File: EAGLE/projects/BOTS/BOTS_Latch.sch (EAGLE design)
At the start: 5 parts, among them J1 T821108A1S100CEU, K1 RT444012

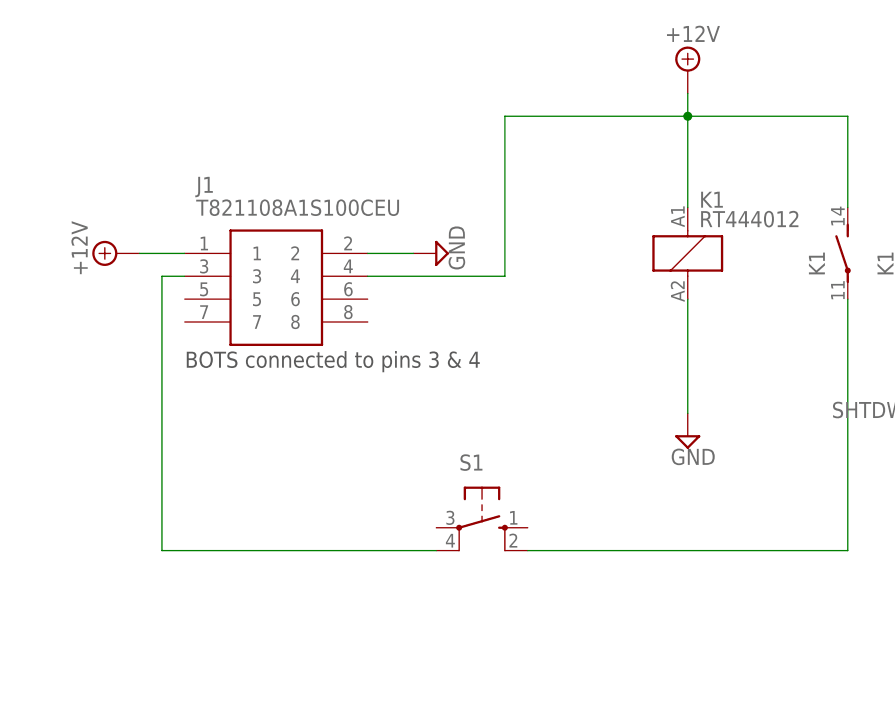
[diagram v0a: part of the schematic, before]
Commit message: Updates to BOTS circuit moving 12v pin to correct position and AMS circuit updates, including library for dual coil relay
Signed-off-by: Jack Bruford <jack.bruford41@gmail.com>
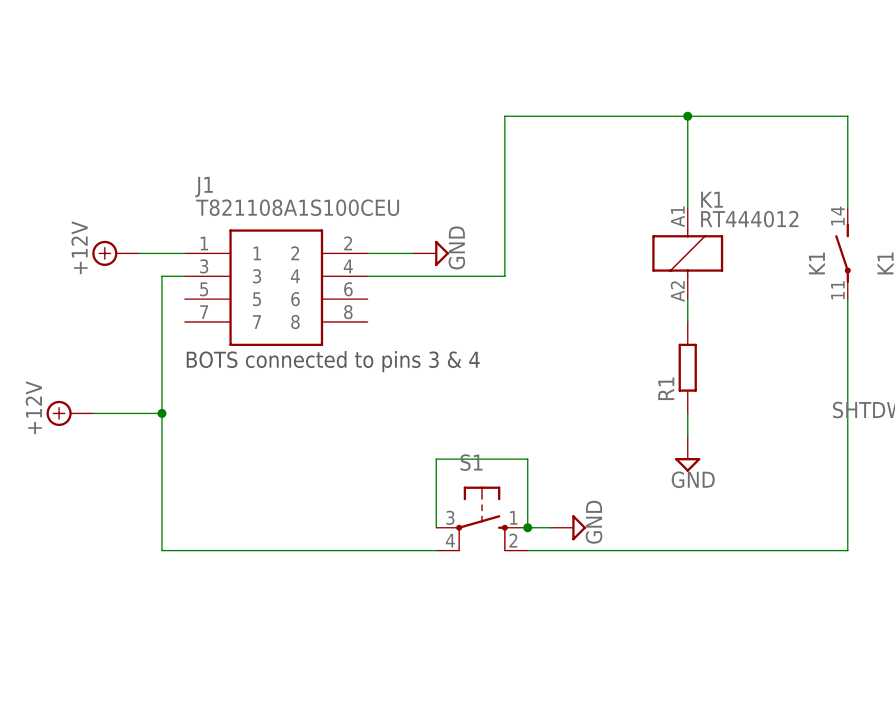
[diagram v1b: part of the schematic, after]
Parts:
- added R1: (no value), rcl:R-EU_0207/15
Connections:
- new net N$5: J1.4, K11.1, K12.S
- net +12V: now also J1.3, S1.P1; no longer J1.4, K11.1, K12.S
- net GND: now also R1.1, S1.P, S1.S; no longer K11.2
- net N$2: now also K11.2, R1.2; no longer J1.3, S1.P1
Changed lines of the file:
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@@
 <layer number="51" name="tDocu" color="7" fill="1" visible="no" active="no"/>
 <layer number="52" name="bDocu" color="7" fill="1" visible="no" active="no"/>
-<layer number="88" name="SimResults" color="9" fill="1" visible="yes" active="yes"/>
+<layer number="88" name="SimResults" color="9" fill="1" visible="no" active="yes"/>
 <layer number="89" name="SimProbes" color="9" fill="1" visible="yes" active="yes"/>
 <layer number="90" name="Modules" color="5" fill="1" visible="yes" active="yes"/>
@@
 <part name="SUPPLY4" library="supply2" library_urn="urn:adsk.eagle:library:372" deviceset="GND" device=""/>
 <part name="S1" library="switch-omron" library_urn="urn:adsk.eagle:library:377" deviceset="10-XX" device="" package3d_urn="urn:adsk.eagle:package:27496/1"/>
+<part name="R1" library="rcl" library_urn="urn:adsk.eagle:library:334" deviceset="R-EU_" device="0207/15" package3d_urn="urn:adsk.eagle:package:23492/1"/>
+<part name="SUPPLY5" library="supply2" library_urn="urn:adsk.eagle:library:372" deviceset="GND" device=""/>
 </parts>
 <sheets>
@@
 <attribute name="VALUE" x="82.55" y="106.68" size="1.778" layer="96" align="center-left"/>
 </instance>
-<instance part="SUPPLY3" gate="+12V" x="137.16" y="121.92" smashed="yes">
-<attribute name="VALUE" x="134.62" y="125.095" size="1.778" layer="96"/>
-</instance>
-<instance part="SUPPLY4" gate="GND" x="137.16" y="81.28" smashed="yes">
-<attribute name="VALUE" x="135.255" y="78.105" size="1.778" layer="96"/>
+<instance part="SUPPLY3" gate="+12V" x="68.58" y="83.82" smashed="yes" rot="R90">
+<attribute name="VALUE" x="65.405" y="81.28" size="1.778" layer="96" rot="R90"/>
+</instance>
+<instance part="SUPPLY4" gate="GND" x="137.16" y="78.74" smashed="yes">
+<attribute name="VALUE" x="135.255" y="75.565" size="1.778" layer="96"/>
 </instance>
 <instance part="S1" gate="1" x="114.3" y="71.12" smashed="yes" rot="R270">
 <attribute name="NAME" x="111.76" y="77.47" size="1.778" layer="95"/>
 <attribute name="VALUE" x="117.475" y="74.93" size="1.778" layer="96"/>
+</instance>
+<instance part="R1" gate="G$1" x="137.16" y="88.9" smashed="yes" rot="R90">
+<attribute name="NAME" x="135.6614" y="85.09" size="1.778" layer="95" rot="R90"/>
+<attribute name="VALUE" x="140.462" y="85.09" size="1.778" layer="96" rot="R90"/>
+</instance>
+<instance part="SUPPLY5" gate="GND" x="124.46" y="71.12" smashed="yes" rot="R90">
+<attribute name="VALUE" x="127.635" y="69.215" size="1.778" layer="96" rot="R90"/>
 </instance>
 </instances>
@@
 <wire x1="76.2" y1="101.6" x2="81.28" y2="101.6" width="0.1524" layer="91"/>
 </segment>
+<segment>
+<pinref part="J1" gate="G$1" pin="3"/>
+<wire x1="81.28" y1="99.06" x2="78.74" y2="99.06" width="0.1524" layer="91"/>
+<wire x1="78.74" y1="68.58" x2="78.74" y2="83.82" width="0.1524" layer="91"/>
+<pinref part="S1" gate="1" pin="P1"/>
+<wire x1="78.74" y1="83.82" x2="78.74" y2="99.06" width="0.1524" layer="91"/>
+<wire x1="78.74" y1="68.58" x2="109.22" y2="68.58" width="0.1524" layer="91"/>
+<pinref part="SUPPLY3" gate="+12V" pin="+12V"/>
+<wire x1="71.12" y1="83.82" x2="78.74" y2="83.82" width="0.1524" layer="91"/>
+<junction x="78.74" y="83.82"/>
+</segment>
+</net>
+<net name="GND" class="0">
+<segment>
+<pinref part="J1" gate="G$1" pin="2"/>
+<pinref part="SUPPLY2" gate="GND" pin="GND"/>
+<wire x1="101.6" y1="101.6" x2="106.68" y2="101.6" width="0.1524" layer="91"/>
+</segment>
+<segment>
+<pinref part="SUPPLY4" gate="GND" pin="GND"/>
+<pinref part="R1" gate="G$1" pin="1"/>
+<wire x1="137.16" y1="81.28" x2="137.16" y2="83.82" width="0.1524" layer="91"/>
+</segment>
+<segment>
+<pinref part="S1" gate="1" pin="S"/>
+<pinref part="SUPPLY5" gate="GND" pin="GND"/>
+<wire x1="119.38" y1="71.12" x2="121.92" y2="71.12" width="0.1524" layer="91"/>
+<wire x1="119.38" y1="71.12" x2="119.38" y2="78.74" width="0.1524" layer="91"/>
+<junction x="119.38" y="71.12"/>
+<wire x1="119.38" y1="78.74" x2="109.22" y2="78.74" width="0.1524" layer="91"/>
+<pinref part="S1" gate="1" pin="P"/>
+<wire x1="109.22" y1="78.74" x2="109.22" y2="71.12" width="0.1524" layer="91"/>
+</segment>
+</net>
+<net name="N$3" class="0">
+<segment>
+<pinref part="SHTDWN+" gate="G$1" pin="TP"/>
+<pinref part="K1" gate="3" pin="S"/>
+<wire x1="162.56" y1="114.3" x2="162.56" y2="106.68" width="0.1524" layer="91"/>
+</segment>
+</net>
+<net name="N$4" class="0">
+<segment>
+<pinref part="SHTDWN-" gate="G$1" pin="TP"/>
+<pinref part="K1" gate="3" pin="P"/>
+<wire x1="162.56" y1="88.9" x2="162.56" y2="96.52" width="0.1524" layer="91"/>
+</segment>
+</net>
+<net name="N$1" class="0">
+<segment>
+<pinref part="K1" gate="2" pin="P"/>
+<wire x1="154.94" y1="96.52" x2="154.94" y2="68.58" width="0.1524" layer="91"/>
+<pinref part="S1" gate="1" pin="S1"/>
+<wire x1="119.38" y1="68.58" x2="154.94" y2="68.58" width="0.1524" layer="91"/>
+</segment>
+</net>
+<net name="N$5" class="0">
 <segment>
 <pinref part="J1" gate="G$1" pin="4"/>
@@
 <wire x1="116.84" y1="116.84" x2="137.16" y2="116.84" width="0.1524" layer="91"/>
 <junction x="137.16" y="116.84"/>
-<pinref part="SUPPLY3" gate="+12V" pin="+12V"/>
-<wire x1="137.16" y1="119.38" x2="137.16" y2="116.84" width="0.1524" layer="91"/>
-</segment>
-</net>
-<net name="GND" class="0">
-<segment>
-<pinref part="J1" gate="G$1" pin="2"/>
-<pinref part="SUPPLY2" gate="GND" pin="GND"/>
-<wire x1="101.6" y1="101.6" x2="106.68" y2="101.6" width="0.1524" layer="91"/>
-</segment>
+</segment>
+</net>
+<net name="N$2" class="0">
 <segment>
 <pinref part="K1" gate="1" pin="2"/>
-<pinref part="SUPPLY4" gate="GND" pin="GND"/>
-<wire x1="137.16" y1="96.52" x2="137.16" y2="83.82" width="0.1524" layer="91"/>
-</segment>
-</net>
-<net name="N$3" class="0">
-<segment>
-<pinref part="SHTDWN+" gate="G$1" pin="TP"/>
-<pinref part="K1" gate="3" pin="S"/>
-<wire x1="162.56" y1="114.3" x2="162.56" y2="106.68" width="0.1524" layer="91"/>
-</segment>
-</net>
-<net name="N$4" class="0">
-<segment>
-<pinref part="SHTDWN-" gate="G$1" pin="TP"/>
-<pinref part="K1" gate="3" pin="P"/>
-<wire x1="162.56" y1="88.9" x2="162.56" y2="96.52" width="0.1524" layer="91"/>
-</segment>
-</net>
-<net name="N$2" class="0">
-<segment>
-<pinref part="J1" gate="G$1" pin="3"/>
-<wire x1="81.28" y1="99.06" x2="78.74" y2="99.06" width="0.1524" layer="91"/>
-<wire x1="78.74" y1="68.58" x2="78.74" y2="99.06" width="0.1524" layer="91"/>
-<pinref part="S1" gate="1" pin="P1"/>
-<wire x1="78.74" y1="68.58" x2="109.22" y2="68.58" width="0.1524" layer="91"/>
-</segment>
-</net>
-<net name="N$1" class="0">
-<segment>
-<pinref part="K1" gate="2" pin="P"/>
-<wire x1="154.94" y1="96.52" x2="154.94" y2="68.58" width="0.1524" layer="91"/>
-<pinref part="S1" gate="1" pin="S1"/>
-<wire x1="119.38" y1="68.58" x2="154.94" y2="68.58" width="0.1524" layer="91"/>
+<wire x1="137.16" y1="96.52" x2="137.16" y2="93.98" width="0.1524" layer="91"/>
+<pinref part="R1" gate="G$1" pin="2"/>
 </segment>
 </net>
@@
 packages will not be understood (or retained) with this version.
 </note>
+<note version="8.4" severity="warning">
+Since Version 8.4, EAGLE supports properties for SPICE simulation.
+Probes in schematics and SPICE mapping objects found in parts and library devices
+will not be understood with this version. Update EAGLE to the latest version
+for full support of SPICE simulation.
+</note>
 </compatibility>

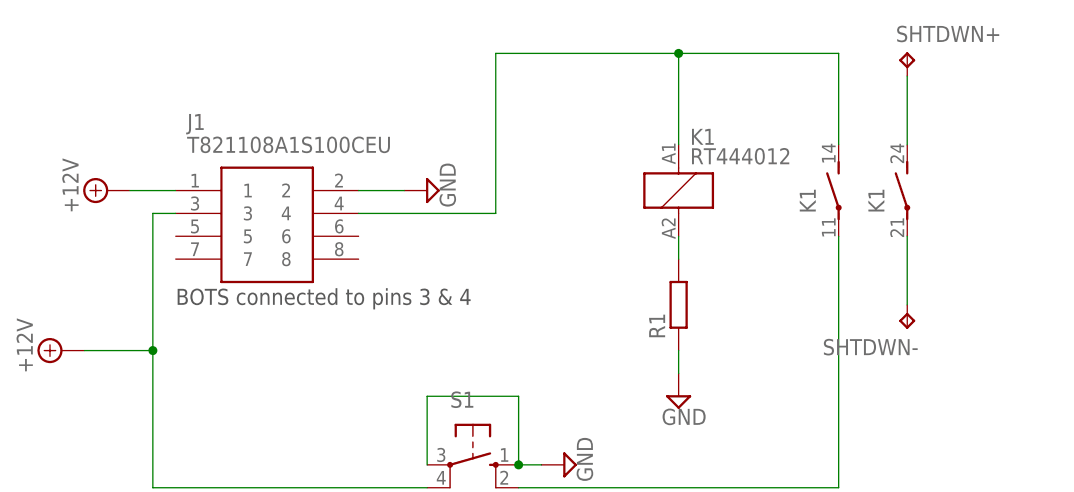
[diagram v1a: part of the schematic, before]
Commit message: BOTS revision so that ESDC goes through connector
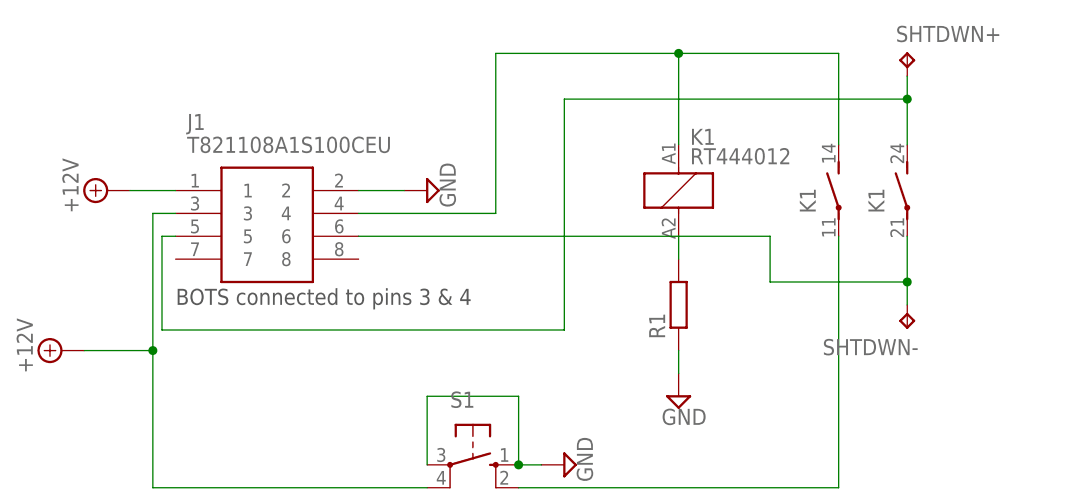
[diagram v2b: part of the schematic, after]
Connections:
- net N$3: now also J1.5
- net N$4: now also J1.6
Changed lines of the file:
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@@
 <pinref part="SHTDWN+" gate="G$1" pin="TP"/>
 <pinref part="K1" gate="3" pin="S"/>
-<wire x1="162.56" y1="114.3" x2="162.56" y2="106.68" width="0.1524" layer="91"/>
+<wire x1="162.56" y1="114.3" x2="162.56" y2="111.76" width="0.1524" layer="91"/>
+<wire x1="162.56" y1="111.76" x2="162.56" y2="106.68" width="0.1524" layer="91"/>
+<wire x1="162.56" y1="111.76" x2="124.46" y2="111.76" width="0.1524" layer="91"/>
+<junction x="162.56" y="111.76"/>
+<wire x1="124.46" y1="111.76" x2="124.46" y2="86.106" width="0.1524" layer="91"/>
+<wire x1="124.46" y1="86.106" x2="79.756" y2="86.106" width="0.1524" layer="91"/>
+<pinref part="J1" gate="G$1" pin="5"/>
+<wire x1="79.756" y1="86.106" x2="79.756" y2="96.52" width="0.1524" layer="91"/>
+<wire x1="79.756" y1="96.52" x2="81.28" y2="96.52" width="0.1524" layer="91"/>
 </segment>
 </net>
@@
 <pinref part="SHTDWN-" gate="G$1" pin="TP"/>
 <pinref part="K1" gate="3" pin="P"/>
-<wire x1="162.56" y1="88.9" x2="162.56" y2="96.52" width="0.1524" layer="91"/>
+<wire x1="162.56" y1="88.9" x2="162.56" y2="91.44" width="0.1524" layer="91"/>
+<pinref part="J1" gate="G$1" pin="6"/>
+<wire x1="162.56" y1="91.44" x2="162.56" y2="96.52" width="0.1524" layer="91"/>
+<wire x1="101.6" y1="96.52" x2="147.32" y2="96.52" width="0.1524" layer="91"/>
+<wire x1="147.32" y1="96.52" x2="147.32" y2="91.44" width="0.1524" layer="91"/>
+<wire x1="147.32" y1="91.44" x2="162.56" y2="91.44" width="0.1524" layer="91"/>
+<junction x="162.56" y="91.44"/>
 </segment>
 </net>
